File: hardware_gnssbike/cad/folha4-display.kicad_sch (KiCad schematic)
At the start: 11 parts, among them J401 Hirose FH28-10S-0.5SH, J402 Molex 503480-0500, Q401 DMG1012T-7

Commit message: feat(hardware): the test points, a readable silkscreen, and paper that fits
Eleven of the sixteen test points of 06-conectores-e-pontos-de-teste.md were
not on the board. Only the three of the console sheet existed; a rail you
cannot put a probe on is a rail you cannot debug. VBUS, VBUSOUT, VBAT, VSYS,
3V0, 1V8, SD3V0, 3V3BL, VBCKP, VINT and the ground reference are there now,
each beside the thing it measures, and each takes what is LEFT: placed with
the rest of JUNTO they pushed three decoupling capacitors off their rings,
one of them to 4.0 mm from a pin that wants 2. The two that are still
missing are the document's own absences - TP111 measures ST_STO, which the
AEM10900 datasheet does not have, and TP401 measures 5V0, from a regulator
not fitted with the JDI panel. The list lives in parts.TESTE and nets.py
refuses a point that names a net that does not exist.

The silkscreen named nothing. Every reference sat 1.8 mm above its part at
0.7 mm with a 0.1 mm stroke - below the floor every fab publishes - and 37
pairs of designators printed on top of each other. The text is at the fab
minimum now, 0.8 mm with 0.15, and each label is PLACED: candidates around
its own courtyard, nearest first, never over another label and preferably
not over another part's outline. 127 references, 0 overlapping. The mounting
hole's REF** is hidden; it names nothing and was the last label sitting on
another.

Ground: a mesh, not just a hem. Edge stitching keeps the boundary of the
surface pours from becoming a radiating slot and does nothing for the
middle, where a patch of pour that reaches the inner plane through a via
20 mm away is not ground at 2.4 GHz. A 4.0 mm grid of ground vias now
covers the board - under the 6.1 mm that is a tenth of a wavelength in
FR-4 - laid last, on what is free, so a stitch never costs a connection.

The router's search learned about pad fields. The neck beside a pad existed
only in emitir(), and emitir only ever sees paths the search already found,
so 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
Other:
- moved on the sheet: C404, J401, J402, JP401, Q401, R401, R402, R403, R404, R405

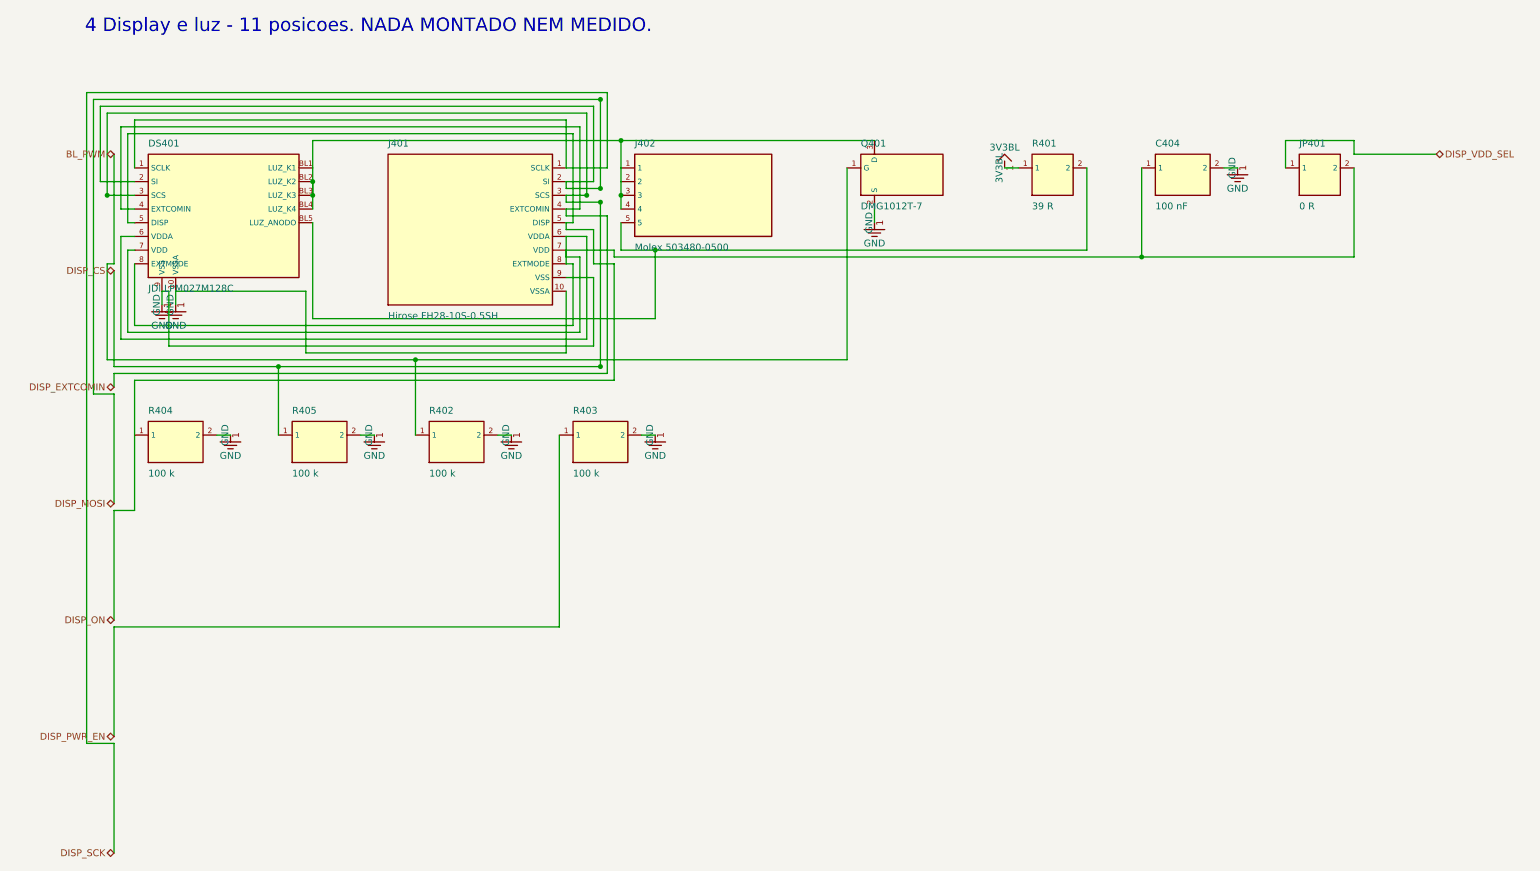
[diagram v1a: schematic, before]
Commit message: feat(hardware): draw each part as its own symbol, not as a block
A rectangle with pin names down its sides is how an INTEGRATED CIRCUIT is
drawn, and only an integrated circuit. This generator drew all 127 parts
that way - resistors, ceramic capacitors, diodes, the TVS - and a sheet of
blocks joined by lines does not show a circuit.

Every class has its own symbol now, in the standard form, with the lead
axis on x and the body between -1.27 and +1.27 mm: a zigzag for a resistor
and a 0 ohm link (42 of them), two parallel plates for a ceramic capacitor
and a curved plate with a + for an electrolytic (31), four arcs for an
inductor (4), the same arcs inside a rectangle for a ferrite bead, which is
what tells the two apart, a zigzag with a diagonal arrow for the thermistor,
a triangle and a bar for a diode with arrows leaving it for an LED, two
contacts with a bar and a plunger for a key, a circle with a diagonal for
the buzzer, and a circle on the end of a lead for a test point. The 36 that
stay rectangles are the ones that should be: the ICs, the connectors and the
display. A two terminal part no longer prints pin numbers or pin names -
"1" and "2" on a resistor is noise, and the symbol already says which end is
which where it matters.

The power symbols had room reserved for the symbol and none for its NAME:
two ground pins two grid steps apart each got their own symbol, the symbols
did not collide, and the words printed over each other - "GNDGNDGND" along
the bottom of every chip. What is reserved now is the whole thing. With a
limit: the first cut let the stub run to fourteen grid steps looking for a
clear spot, and one of them crossed a component and split a net. A long stub
is worse than a crowded label, so it stops at eight and the label gives way.

One attempt is NOT in this commit, on purpose. Grouping every pin of a rail
on one edge into a single symbol - which is what a person draws - joins the
stubs with a line that runs along the part's edge and crosses w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
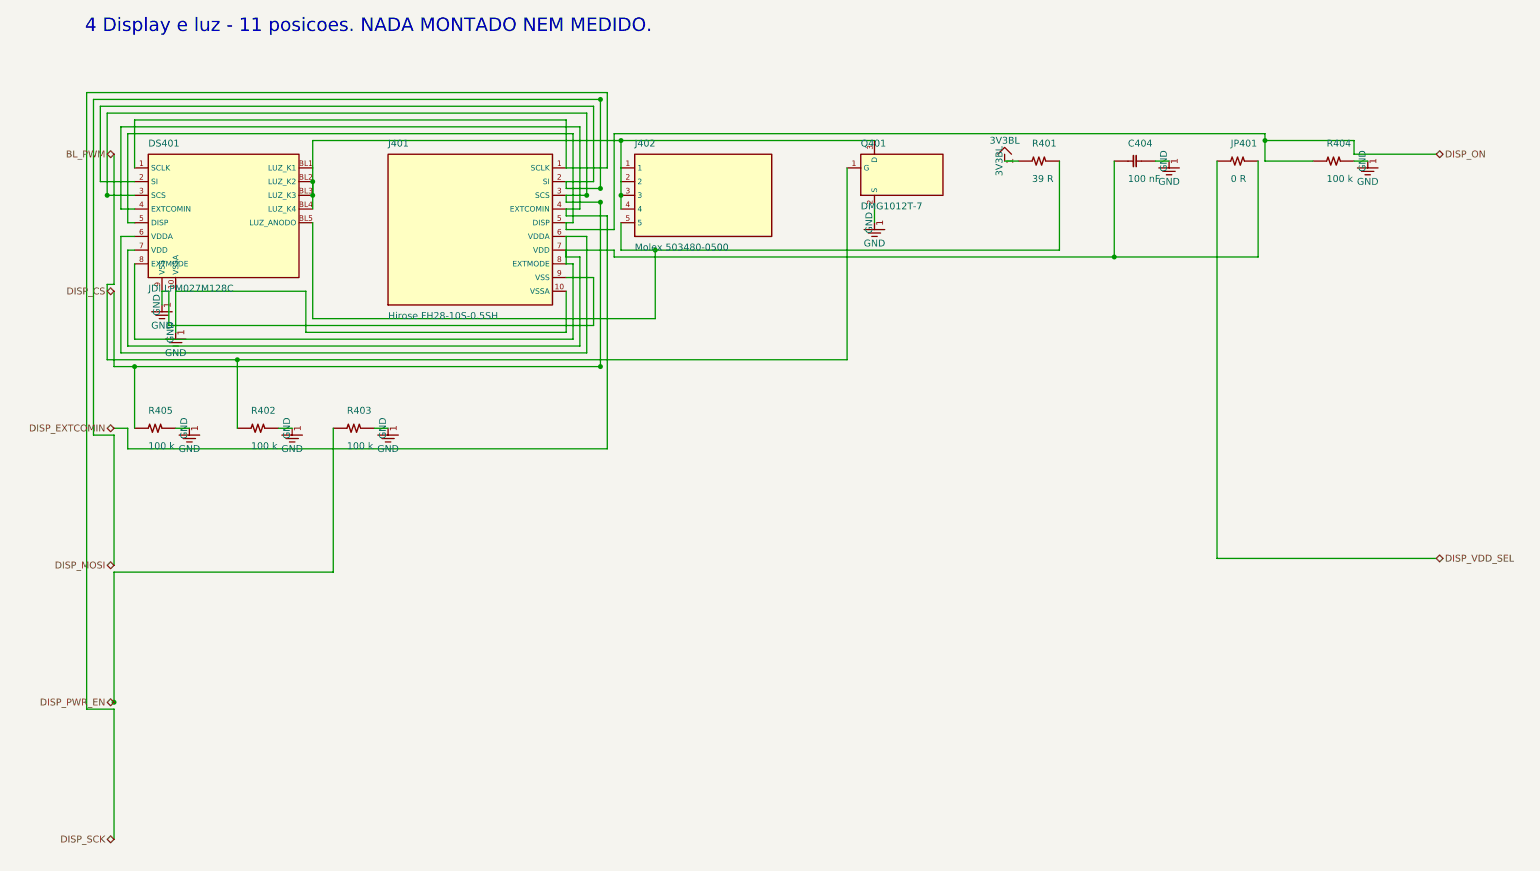
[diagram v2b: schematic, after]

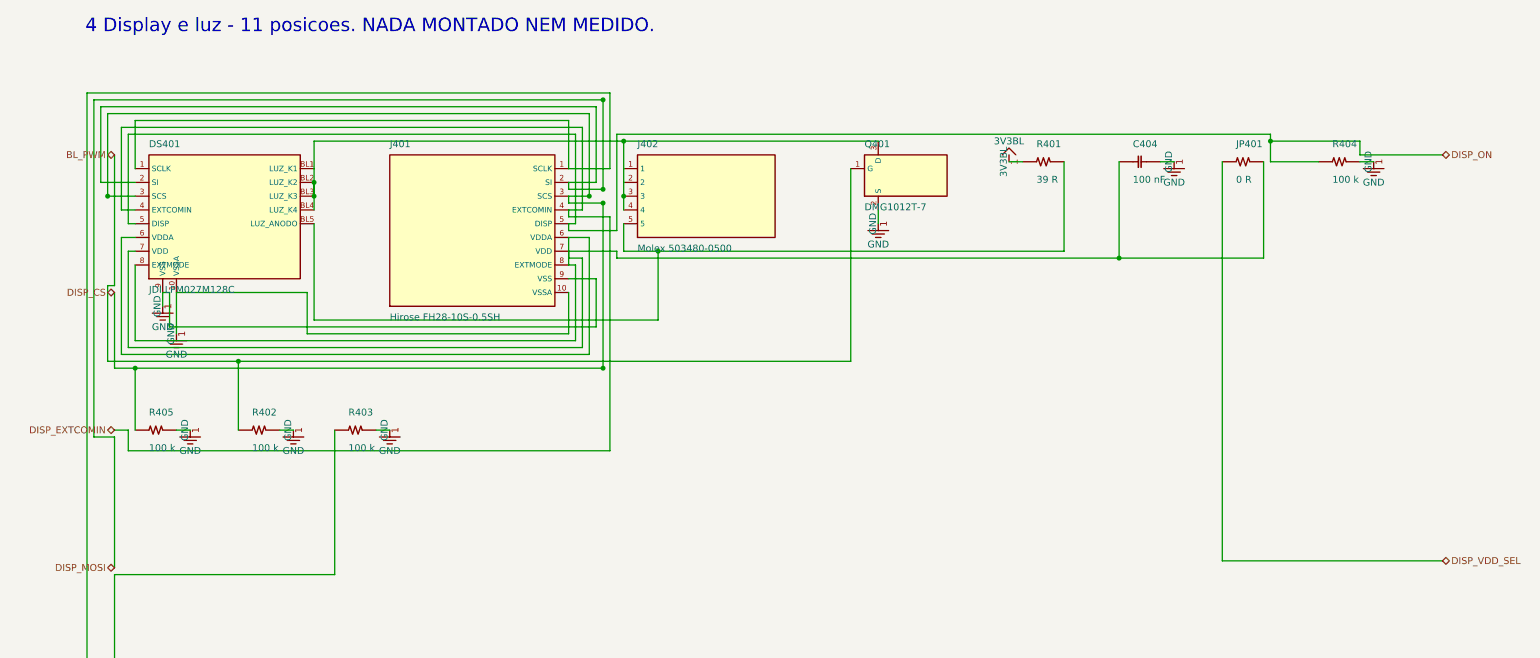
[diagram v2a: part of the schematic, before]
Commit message: feat(hardware): the GNSS antenna comes onto the board, and the cut-out shrinks
The TE L000670-01 is zero at LCSC, and it was never going to work here
anyway: it asked for 40,5 x 14,5 mm with no copper on ANY layer, which is
wider than this whole 34 mm board, and its own efficiency curve collapsed
with a short ground plane - 62 % in L5 at 90 mm of ground, 43 % at 70,
29 % at 50. L5 is the entire reason the MAX-F10S was chosen.

The Unictron H2UJ4U1H2Q0100 (C6569550, 5.491 in stock) replaces it. Its
cut-out is 15,00 x 9,35 mm on the top layer and 15,00 x 9,88 on the
bottom, measured from the BOARD EDGE, and the part is 5,0 x 3,0 x 0,5 mm
against 14 x 10,75 x 1.

E301 was the only part still living outside the board: it had no
footprint, so the jumper's CHIP branch went to something that was not
laid out. It now has a land pattern read off the layout guide - two
ground/tuning pads of 0,80 x 2,98 straddling the ends, 0,40 under the
body and 0,40 outside for the fillet to climb the wrap-around
metallisation, and a 1,00 x 2,00 signal pad at the geometric centre -
and it sits on the bottom edge, 0,30 mm from it.

Its two end pads are ground AND tuning: they reach the plane through
C305 and C306, positions [8] and [9] of the data sheet's network, not
directly. The matching network's values changed with the antenna: the
shunt is 1,5 pF, the series element becomes a 3,6 pF CAPACITOR instead
of a 3,9 nH inductor, and the second shunt is not fitted. Same 0402
land patterns, so the board does not change - only what is soldered on
it, and it changes again if the u.FL branch is the one fitted.

The cut-out is 20,08 mm wide and not the data sheet's 15,00, and that is
deliberate: the cut-out is asymmetric about the antenna - 2,46 mm one
side and 7,54 the other - and which side is which is not determined.
Applying 7,54 to both sides meets the requirement whichever way the part
faces. It costs about 5 mm of ground plane on an antenna that depends on
it, and it can go back to 15,00 onc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
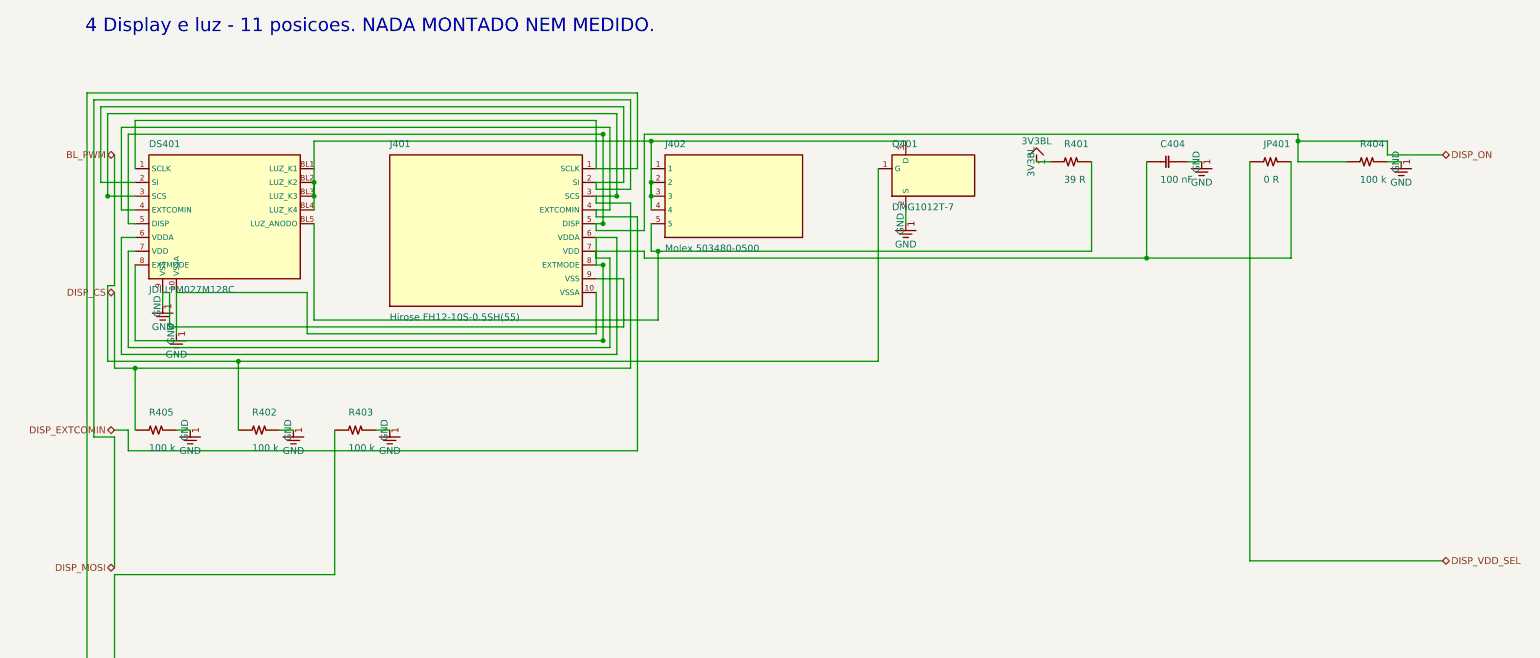
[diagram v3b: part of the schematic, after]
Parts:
- J401: value Hirose FH28-10S-0.5SH -> Hirose FH12-10S-0.5SH(55)
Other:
- moved on the sheet: C404, J401, J402, JP401, Q401, R401, R404
